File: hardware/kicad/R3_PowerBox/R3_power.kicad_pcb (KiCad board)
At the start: 4 copper layers, 160 x 80 mm, 199 parts, among them J1 SERVICE / BENCH INPUT 6-12V, J10 BATTERY / CHARGER TELEMETRY, J11 USER PANEL / PRIMARY ONLY, J12 PRIMARY B2B 2x8 / DNP, J13 ISOLATED B2B 2x5 / DNP, J2 DIGITAL POWER OUT, J3 ISOLATED POWER OUT, J4 CONTROL / SERVICE, J5 PRIMARY AUX DNP, J6 ISOLATED AUX DNP, J7 USB-C POWER INPUT, J8 2S BATTERY / KEYED / NTC_BMS=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, J9 NTC_CHG=103AT-2 / QUIET DGND 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, Q1 DMP3007LSS-13, Q2 CSD17577Q3AT 30V NMOS DSG, Q3 CSD17577Q3AT 30V NMOS CHG, Q4 DMP3007LSS-13 SYSTEM LOAD SWI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, SW1 C&K RS282G05A3 / POWER ON, SW2 QON SERVICE / TL3305AF160QG, U1 TPS62132RGTR, U10 STUSB4500QTR, U11 BQ294502 SPACE ONLY / NC / DNP, U2 TPS54302DDCR, U3 RS3E-0505S/H3, U4 ADM7150ACPZ-3.3-R7, U5 TPS7A2033PDBVR, U6 RS3-0505D/H3, U7 TPS2121RUXR, U8 BQ25798RQM, U9 BQ28Z610DRZR

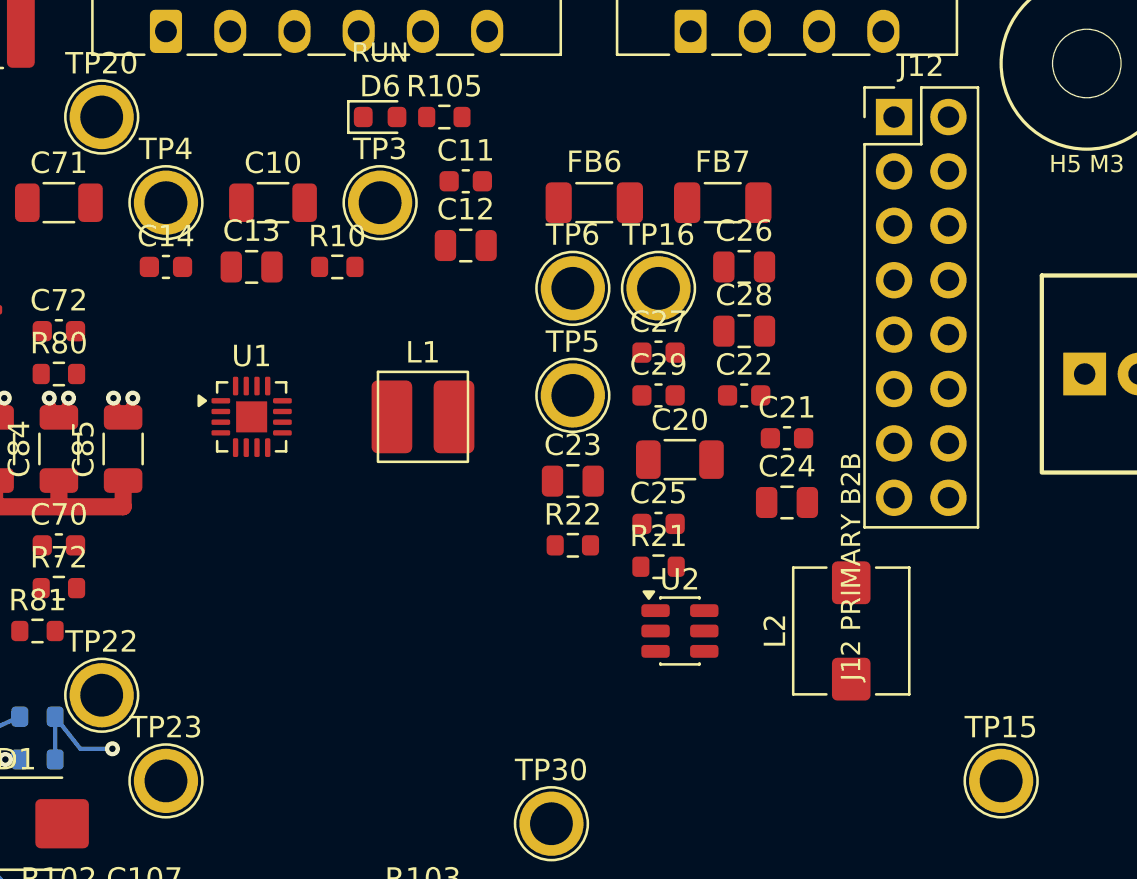
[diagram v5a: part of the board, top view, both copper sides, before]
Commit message: Route checkpoint B local TPS62132 and TPS54302 converters
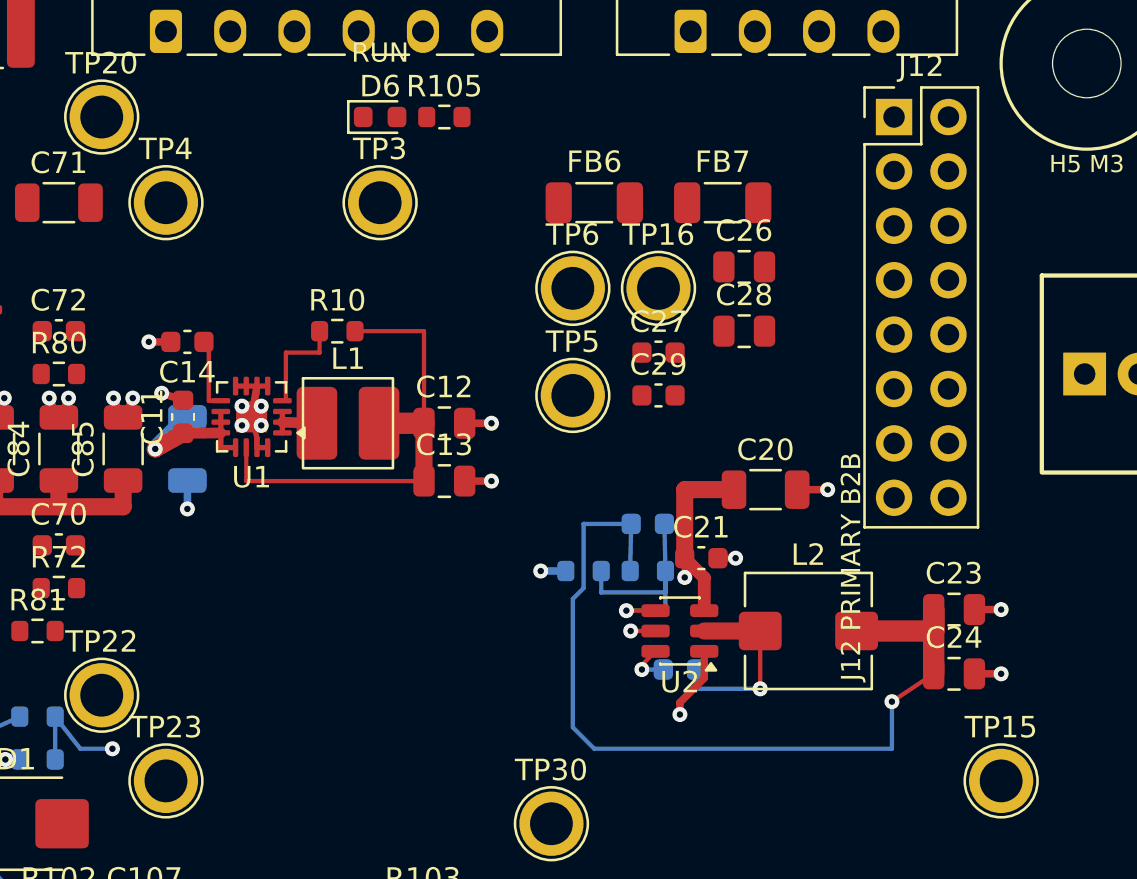
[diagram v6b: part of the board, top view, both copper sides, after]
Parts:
- C10, C22, C25, R21, R22: moved to B.Cu
- moved C23 18.8 mm to (108.8, 51.0)
- moved C11 17.2 mm to (72.8, 42.0), turned to 90 degrees
- moved C13 13.5 mm to (85.0, 45.0)
- moved C22 13.1 mm to (96.0, 53.8)
- moved C10 12.2 mm to (73.0, 43.5), turned to -90 degrees
- moved C24 11.2 mm to (108.8, 54.0)
- moved C12 8.36 mm to (85.0, 42.3)
- moved C21 6.88 mm to (97.0, 48.6)
- moved C20 4.24 mm to (100.0, 45.4)
- moved C14 3.64 mm to (73.0, 38.5), turned to 180 degrees
- moved L1 3.51 mm to (80.5, 42.3)
- moved R10 3.00 mm to (80.0, 38.0)
- moved L2 2.00 mm to (102.0, 52.0), turned to 0 degrees
- moved R22 1.30 mm to (91.5, 49.2), turned to 180 degrees
- moved R21 0.54 mm to (94.5, 49.2)
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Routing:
- net +5V_PREISO: track 0.00 -> 41.6 mm, vias 0 -> 1
- net +3V3_D: track 0.00 -> 22.2 mm
- net VSYS_MAIN: track 0.00 -> 21.7 mm, vias 0 -> 3
- net DGND: track 60.4 -> 80.6 mm, vias 40 -> 55
- net FB_5V: track 0.00 -> 12.2 mm, vias 0 -> 1
- net SW_5V: track 0.00 -> 9.19 mm, vias 0 -> 1
- net PG_3V3_D: track 0.00 -> 4.99 mm
- net N$11: track 0.00 -> 3.54 mm
- net SW_3V3: track 0.00 -> 2.61 mm
- net N$12: track 0.00 -> 2.11 mm, vias 0 -> 1

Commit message: Route checkpoint C separate isolation feeds and clean LDO rails
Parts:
- C26, C27, C28, C29, C30, C31, FB6, FB7, R40: moved to B.Cu
- moved FB7 39.1 mm to (112.0, 68.5)
- moved C29 36.9 mm to (116.5, 71.0)
- moved C28 35.2 mm to (116.5, 68.5)
- moved FB6 26.6 mm to (112.5, 49.0)
- moved C27 22.8 mm to (116.5, 46.5)
- moved C26 19.7 mm to (116.5, 44.0)
- moved C30 19.1 mm to (128.5, 43.0)
- moved C31 16.1 mm to (132.0, 43.0)
- moved C43 11.3 mm to (148.8, 38.3), turned to 90 degrees
- moved C44 10.6 mm to (142.0, 38.5), turned to 90 degrees
- moved C40 10.3 mm to (148.5, 44.5)
- moved C42 9.66 mm to (140.5, 41.5), turned to 180 degrees
- moved C41 8.28 mm to (141.5, 44.5), turned to 180 degrees
- moved R40 3.91 mm to (148.0, 45.5)
- moved C50 1.58 mm to (140.5, 65.5), turned to 180 degrees
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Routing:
- net +5V_PREISO: track 41.6 -> 81.8 mm, vias 1 -> 7
- net +5V_ISO_A: track 0.00 -> 30.8 mm, vias 0 -> 2
- net +5V_ISO_D: track 0.00 -> 30.0 mm, vias 0 -> 2
- net -5V_INA_RAW: track 0.00 -> 26.2 mm, vias 0 -> 1
- net GND_ISO: track 0.00 -> 24.3 mm, vias 0 -> 22
- net +5V_ISO_RAW: track 0.00 -> 20.0 mm, vias 0 -> 1
- net +5V_PREISO_ADS: track 0.00 -> 10.2 mm
- net -5V_INA: track 0.00 -> 9.54 mm
- net +5V_PREISO_INA: track 0.00 -> 7.10 mm
- net +5V_INA: track 0.00 -> 6.14 mm
- net +5V_INA_RAW: track 0.00 -> 6.02 mm
- net EN_3V3_A_ISO: track 0.00 -> 5.91 mm, vias 0 -> 1
- net DGND: track 80.6 -> 85.6 mm, vias 55 -> 59
- net ADM7150_REF: track 0.00 -> 4.13 mm
- net N$14: track 0.00 -> 3.83 mm
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
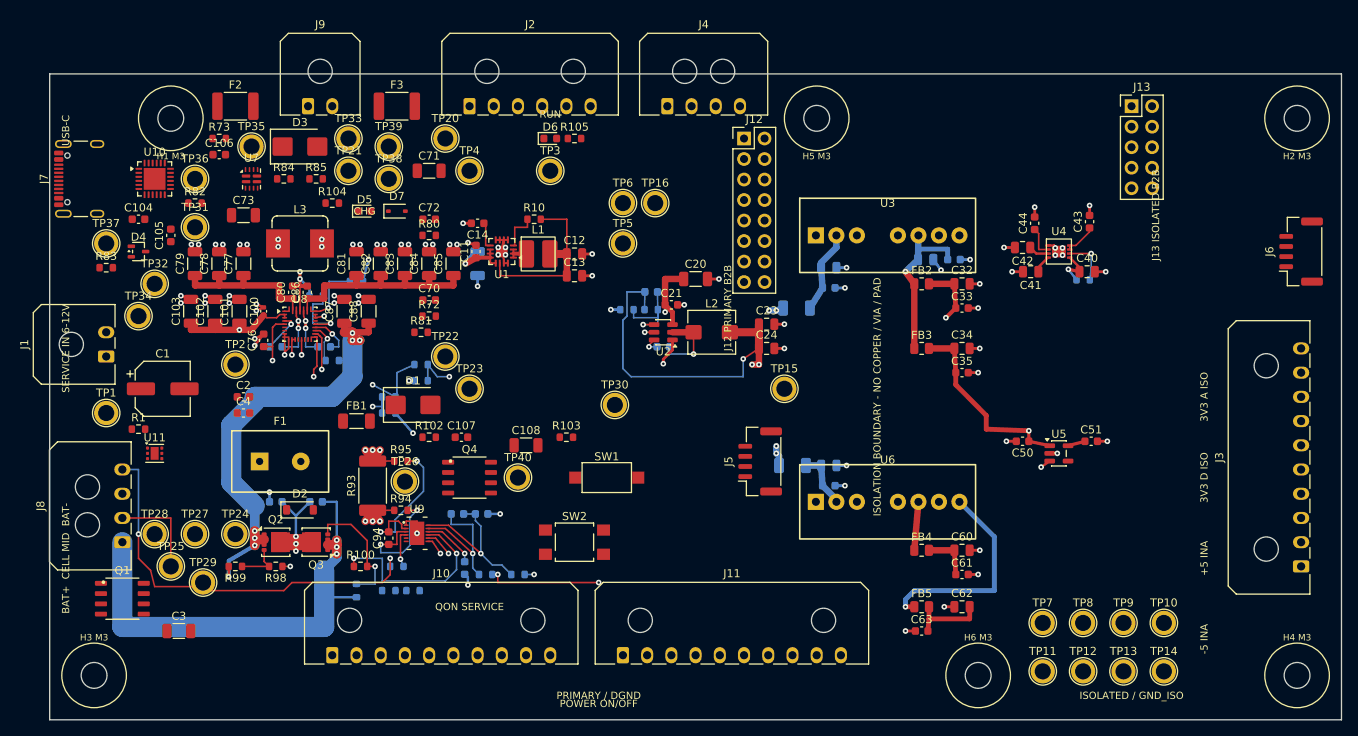
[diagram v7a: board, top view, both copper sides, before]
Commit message: Route R3 checkpoint D interconnect and verified local escapes
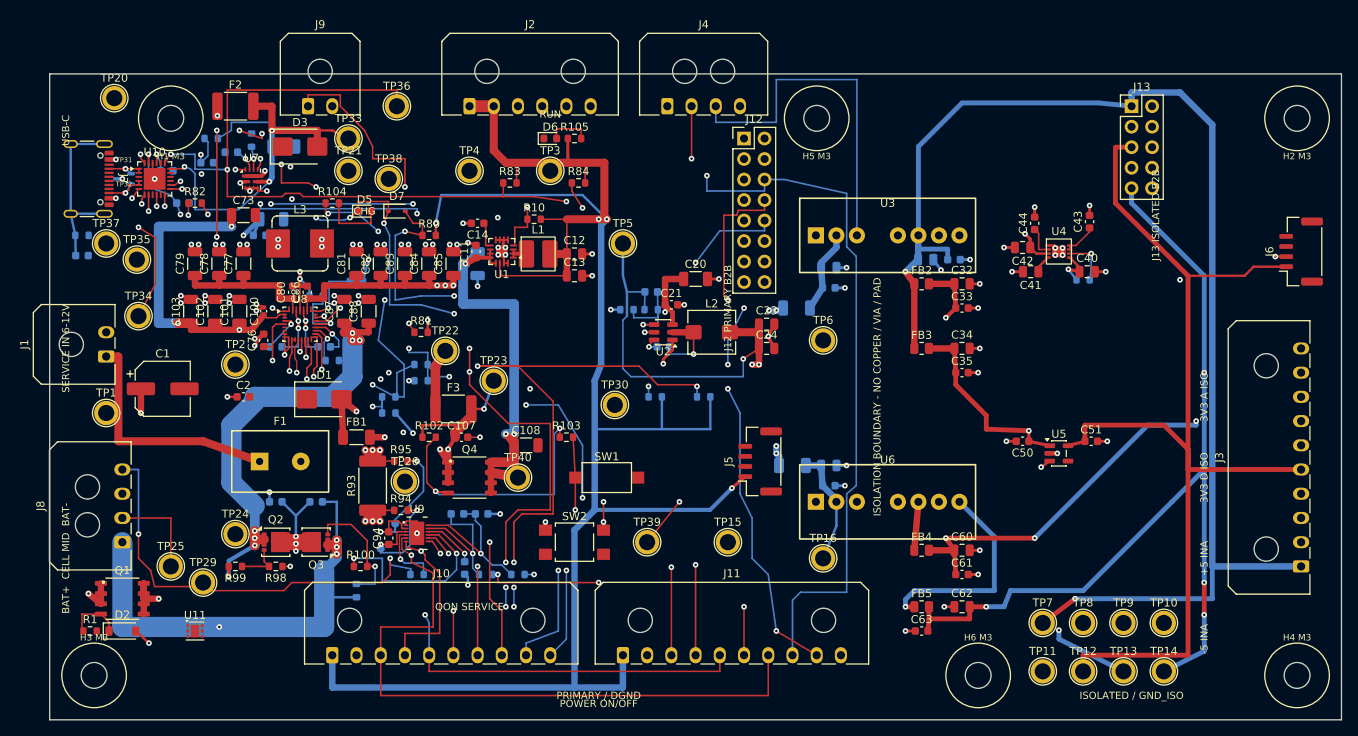
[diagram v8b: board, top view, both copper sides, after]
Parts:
- C104, C105, C106, C3, C4, C70, C71, C72, D4, R72, R73, R85: moved to B.Cu
- TP27, TP28: footprint TestPoint_Plated_Hole_D2.0mm -> TestPoint_Pad_D1.0mm; moved to B.Cu
- TP31, TP32: footprint TestPoint_Plated_Hole_D2.0mm -> R3_Power:TestPoint_CC_D0.6mm
- moved TP39 58.5 mm to (94.0, 78.0)
- moved C3 52.3 mm to (47.5, 38.0)
- moved R83 51.1 mm to (77.0, 33.5)
- moved TP16 48.7 mm to (115.8, 80.0)
- moved R72 44.1 mm to (24.0, 40.0)
- moved C70 43.4 mm to (24.0, 42.5)
- moved R97 43.3 mm to (101.0, 60.0)
- moved TP20 41.3 mm to (28.0, 23.0)
- moved R96 40.8 mm to (95.0, 60.0)
- moved F3 38.1 mm to (70.0, 61.5)
- moved R84 36.5 mm to (85.5, 33.5)
- moved TP6 30.1 mm to (115.8, 53.0)
- moved TP28 29.8 mm to (62.8, 75.7)
- moved D2 26.6 mm to (29.0, 89.0)
- moved TP36 26.6 mm to (63.0, 24.0)
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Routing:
- net PM_I2C_SCL: track 0.00 -> 400.8 mm, vias 0 -> 10
- net PM_I2C_SDA: track 0.00 -> 384.2 mm, vias 0 -> 11
- net +3V3_D: track 22.2 -> 349.5 mm, vias 0 -> 7
- net CHARGE_STATUS: track 0.00 -> 221.8 mm, vias 0 -> 4
- net PD_ALERT_N: track 0.00 -> 213.2 mm, vias 0 -> 4
- net INPUT_SOURCE_STATUS: track 0.00 -> 195.7 mm, vias 0 -> 6
- net PG_3V3_D: track 4.99 -> 193.0 mm, vias 0 -> 4
- net CHARGER_INT_FAULT: track 0.00 -> 177.4 mm, vias 0 -> 3
- net PD_CONTRACT_12V_N: track 0.00 -> 176.7 mm, vias 0 -> 6
- net BQ_STAT_RAW: track 0.00 -> 166.0 mm, vias 0 -> 15
- net QON_SERVICE: track 0.00 -> 161.6 mm, vias 0 -> 9
- net +3V3_A_ISO: track 2.51 -> 149.5 mm, vias 0 -> 3
- net +5V_ISO_RAW: track 20.0 -> 164.7 mm, vias 1 -> 2
- net +3V3_D_ISO: track 2.16 -> 130.9 mm
- net -5V_INA: track 9.54 -> 126.9 mm, vias 0 -> 4
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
